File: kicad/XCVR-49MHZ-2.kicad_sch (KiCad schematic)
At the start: 6 parts, among them J1 JST_GH_06P, J2 SMA_Edge

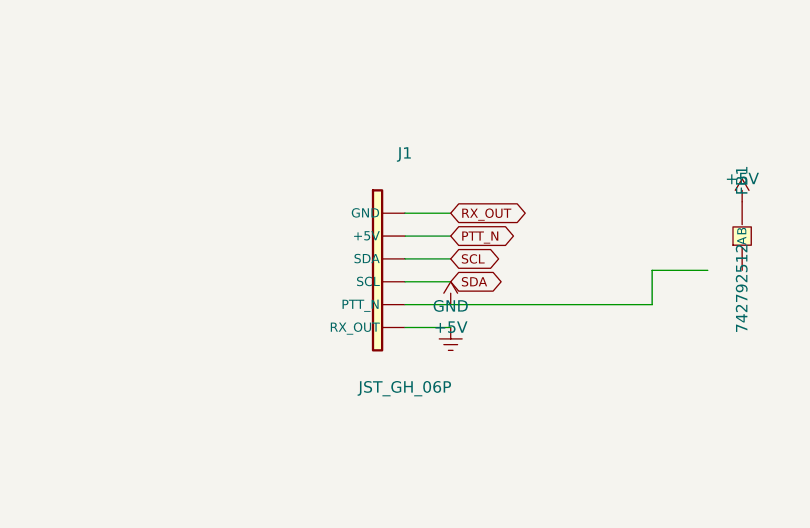
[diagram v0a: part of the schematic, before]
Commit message: Add shielded JST-GH connectors, wiring harness spec, Faraday enclosure, and bay fans
Schematics (Cape-A-2, Cape-B-2, XCVR-49MHZ-2):
- Added SHIELD/MP pin to all JST-GH connector symbol definitions, bonded to PGND
- Added PGND power symbol definition to each schematic's lib_symbols
- Added pin "MP" UUID to all connector instances (J_VBAT, J_SBUS, J_XCVR, J1)
- Added PGND power symbol instance at each connector's MP mounting-tab pad
- Added J_FAN 3-pin JST-GH connector to Cape-A-2 and Cape-B-2
  (GND / +5V / FAN_PWM_A|B + PGND shield bond)
- Added Conn_JST_GH_03P symbol definition to Cape-B-2 lib_symbols

Design docs:
- Cape-A-2.md §9: Shielded JST-GH connector spec (cable type, drain wire, ferrite)
- Cape-A-2.md §10: J_FAN fan connector spec (Sunon MF40100V2, 5 V, PWM)
- Cape-A-2.md §11: Wiring harness requirements — all cables twisted+shielded+ferrite
  (CAN FD / RS-485 / 1553 / PWM / power / Ethernet / SBUS / fan)
- Cape-A-2.md §12: Avionics bay Faraday enclosure — 3M 1181 copper foil liner,
  Laird HCZ0-2050-A 40 mm honeycomb EMC vent, fan frame PGND bond, access-panel
  conductive foam gaskets, cable entry ferrite clamps; SE ≥ 30 dB @ 49 MHz
- Cape-B-2.md: Matching shielded connector spec, J_FAN, wiring requirements,
  Faraday enclosure addenda (XCVR SMA bulkhead, RF antenna pigtail routing)
- XCVR-49MHZ-2.md §8: J1 shielded cable assembly spec, drain wire, ferrite clamp
  placement; SMA antenna cable spec; wiring interaction with on-board CM5/TVS6/FB-TX

Ref: Cape-A-2.md §12.5 (SE budget), IEC 61000-4-2/4-5, MIL-STD-461G RS103

https://claude.ai/code/session_01PLmQi3tDwTStFSfcJLQJp7
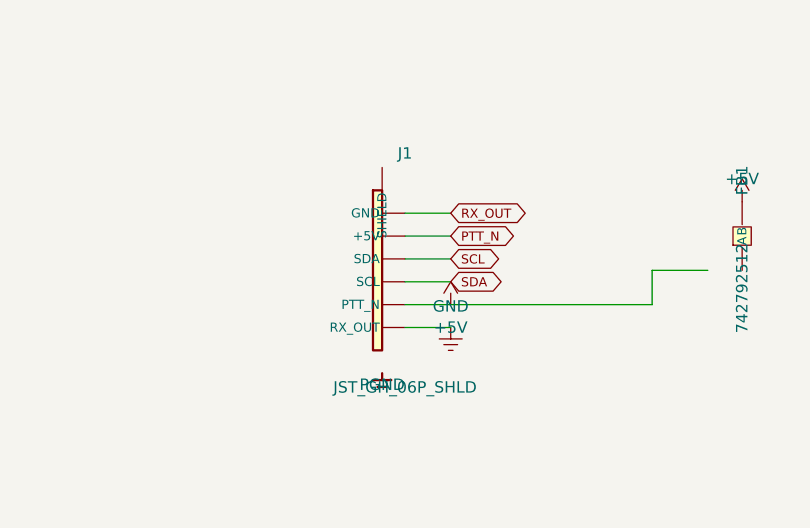
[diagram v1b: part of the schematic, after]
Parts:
- J1: value JST_GH_06P -> JST_GH_06P_SHLD
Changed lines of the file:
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@@
     (property "Reference" "J1" (at 52.54 87.00 0)
       (effects (font (size 1.27 1.27))))
-    (property "Value" "JST_GH_06P" (at 52.54 113.00 0)
+    (property "Value" "JST_GH_06P_SHLD" (at 52.54 113.00 0)
       (effects (font (size 1.27 1.27))))
     (property "Footprint"
@@
     (pin "4")
     (pin "5")
-    (pin "6"))
+    (pin "6")
+    (pin "MP"))
+  ;; PGND at J1 SHIELD (MP) mounting tab — chassis ground bond for cable braid drain
+  (symbol (lib_id "PGND") (at 50.00 111.43 0)
+    (unit 1) (exclude_from_sim no) (in_bom no) (on_board yes) (dnp no)
+    (property "Reference" "#PWR_J1_SHLD" (at 50.00 111.43 0) (effects (font (size 1.27 1.27)) (hide yes)))
+    (property "Value" "PGND" (at 50.00 112.70 0) (effects (font (size 1.27 1.27))))
+    (pin "1"))
   ;; -- FB1: Wurth 742792512 ferrite bead, 600Ω@100MHz 2A, on +5V entry --
   (symbol (lib_id "Ferrite_Bead") (at 90.00 96.19 90)
